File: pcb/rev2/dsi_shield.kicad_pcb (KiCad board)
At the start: 4 copper layers, 68.6 x 53.3 mm, 224 parts, among them CN1 HDMI, CN10 CVBS In, CN2 AX3E41264, CN3 GB042-30S-E1000, CN4 JTAG, CN5 IOH, CN6 POWER, CN7 IOL, CN8 AD, CN9 USB, IC1 XC6SLX9-3TQG144I, IC10 MT46V32M16P-5B:F, IC12 25MHz, IC2 M25P80-VMN6P, IC28 TVP5150AM1PBS, IC3 LV52204MUTBG, IC4 LM26480, IC5 TPS61040, IC6 FT230XS-T, IC8 PRTR5V0U2X, IC9 PRTR5V0U2X, Q1 BSS84, Q2 2N7002, Q3 2N7002, Q4 2N7002, X1 7A-14.31818MAAJ-T

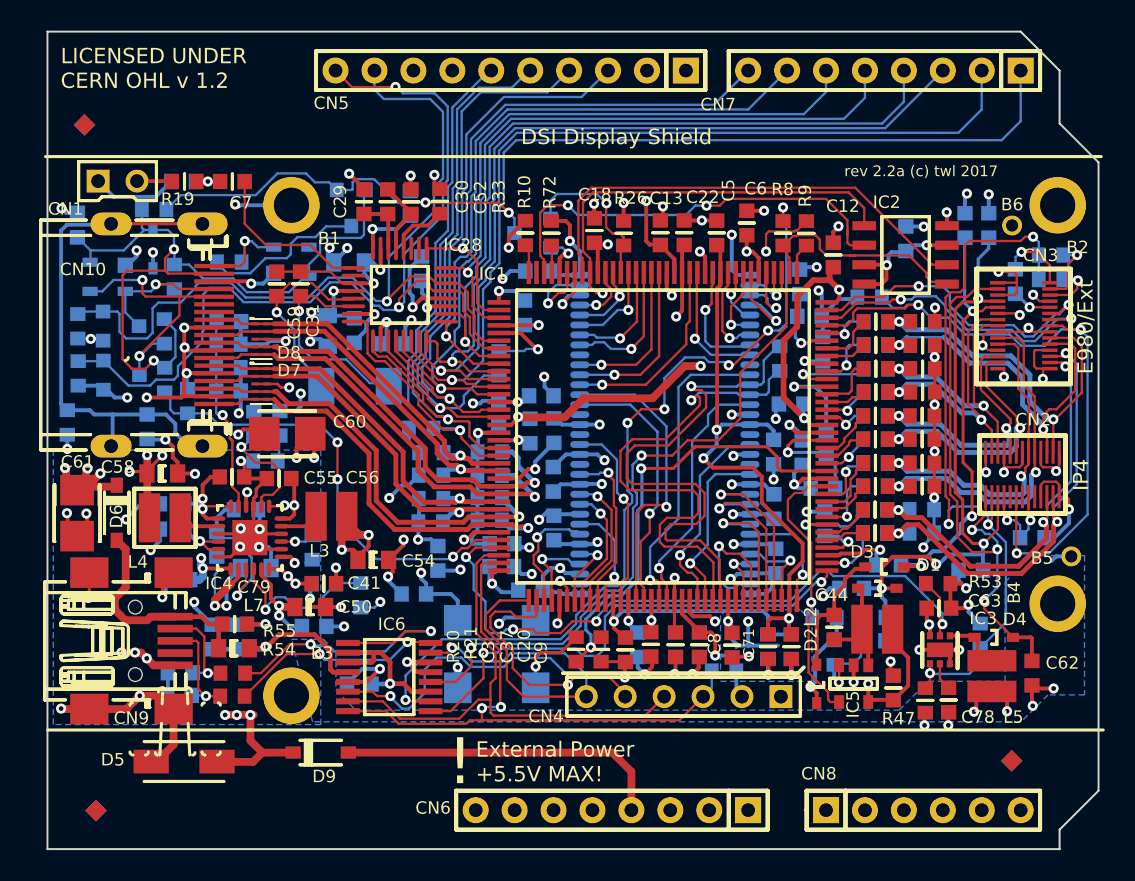
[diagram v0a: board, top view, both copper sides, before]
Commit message: Completed port to KiCad, passes DRC+LVS. NOT MANUFACTURED.
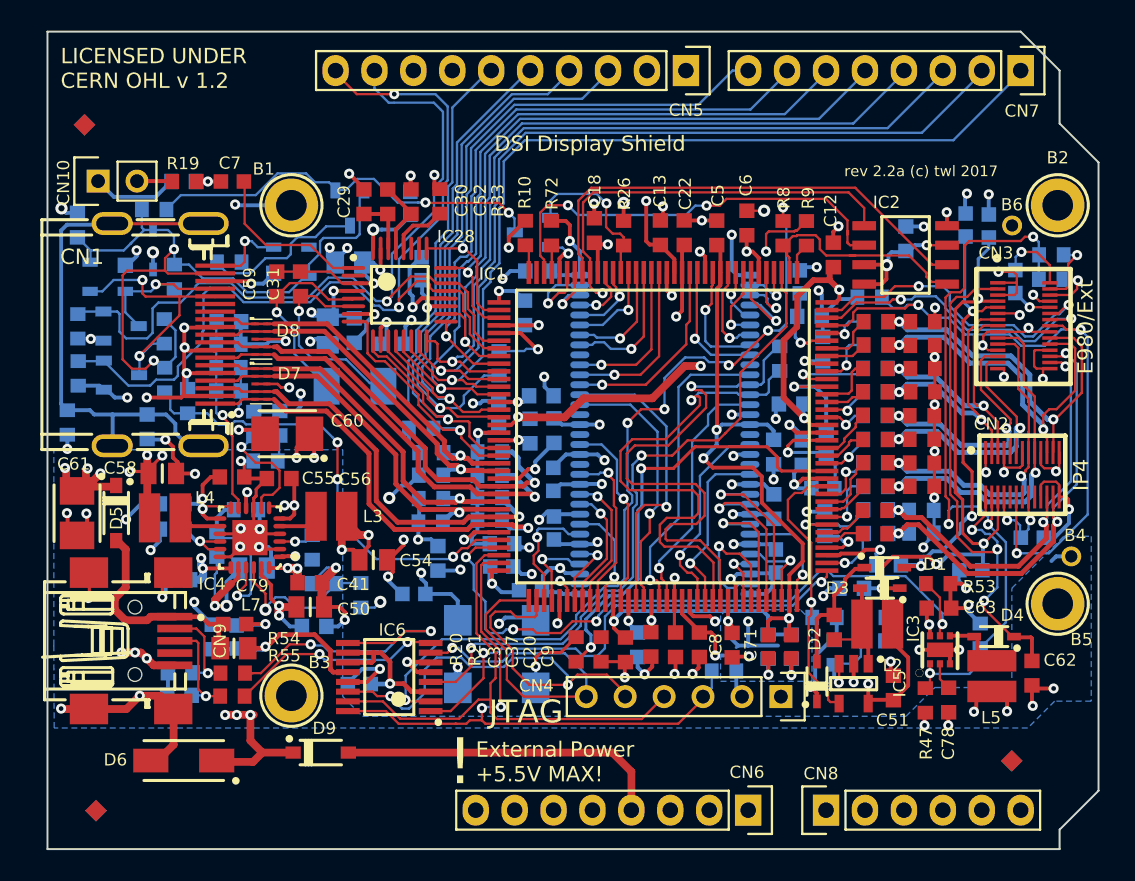
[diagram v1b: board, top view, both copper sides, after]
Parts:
- B1, B2, B3, B4: value Plated Hole -> PLATED_HOLE2.0_PAD3.5; footprint c350h200 -> Pads:c350h200
- B5, B6: value Plated Hole -> PLATED_HOLE0.8_PAD1.3
- C1, C2, C32, C33, C34: value 100n -> CC0603_100NF_100V_10%_X7R; footprint CAPC1608X87N -> CAPC1608X90N
- C10, C12, C13, C15, C16, C18, C20, C21, C22, C23, C25, C27, C28, C3, C35, C36, C37, C38, C4, C40, C5, C8: value 100n -> CC0603_100NF_50V_10%_X7R; footprint CAPC1608X87N -> Capacitors SMD:CAPC1608X87N
- C11, C17, C65, C67, C7, C71, C72, C73, C75, C77, C79, C82, C84, C85, C86: value 100n -> CC0603_100NF_100V_10%_X7R; footprint CAPC1608X87N -> Capacitors SMD:CAPC1608X90N
- C14, C19, C24, C29, C30, C41, C42, C43, C44, C47, C48, C52, C6, C62, C63, C64, C76, C83, C9: value 1u X5R -> CC0603_1UF_50V_10%_X5R; footprint CAPC1608X87N -> Capacitors SMD:CAPC1608X87N
- C26, C39: value 1n -> CC0603_1NF_50V_5%_NP0; footprint CAPC1608X87N -> Capacitors SMD:CAPC1608X90N
- C31, C49, C59: value 22p -> CC0603_22PF_50V_5%_NP0; footprint CAPC1608X87N -> Capacitors SMD:CAPC1608X87N
- C45, C51, C55, C56: value 4.7u X5R -> CC0603_4.7UF_6.3V_10%_X5R; footprint CAPC1608X87N -> Capacitors SMD:CAPC1608X87N
- C46, C50, C54, C58: value 10u X5R -> CC0805_10UF_16V_10%_X5R; footprint INDC2012-0805 -> Capacitors SMD:CAPC2012X135N
- C53: value 8.2p -> CC0603_8.2PF_50V_0.5PF_NP0; footprint CAPC1608X87N -> Capacitors SMD:CAPC1608X87N
- C57: value 6.8p -> CC0603_6.8PF_50V_0.5PF_NP0; footprint CAPC1608X87N -> Capacitors SMD:CAPC1608X87N
- C60, C61: value 47u -> CTE3528-21_47UF_6.3V_10%_LESR0250; footprint TC3528-1411 -> Capacitors SMD:CAPMP3528X210N
- C66, C68, C69, C70: value 10n -> CC0603_10NF_50V_10%_X7R; footprint CAPC1608X87N -> Capacitors SMD:CAPC1608X87N
- C74, C80, C81: value 33p -> CC0603_33PF_50V_5%_NP0; footprint CAPC1608X87N -> Capacitors SMD:CAPC1608X87N
- C78: value 220n -> CC0603_220NF_10V_10%_X7R; footprint CAPC1608X87N -> Capacitors SMD:CAPC1608X87N
- CN1: value HDMI -> MOLEX_500254-1927
- CN10: footprint HDR1X2 -> Pin_Headers:Pin_Header_Straight_1x02
- CN2: footprint IPHONE4_LCD_CONN -> dsi_shield:IPHONE4_LCD_CONN
- CN3: value GB042-30S-E1000 -> CONN_02X15_ALT; footprint GB042-30S-E1000 -> dsi_shield:GB042-30S-E1000
- CN4: footprint HDR1X6 -> Pin_Headers:Pin_Header_Straight_1x06
- CN5: footprint Header 10x1 8.5mm -> Pin_Headers:Pin_Header_Straight_1x10
- CN6: value POWER -> POWER_UNO; footprint Header 8x1 8.5mm -> Pin_Headers:Pin_Header_Straight_1x08
- CN7: footprint Header 8x1 8.5mm -> Pin_Headers:Pin_Header_Straight_1x08
- CN8: footprint Header 6x1 8.5mm -> Pin_Headers:Pin_Header_Straight_1x06
- CN9: value USB -> TYCO_1734035-1; footprint TYCO_1734035-1 -> TYCO SMD:TYCO_1734035-1
- D1, D2, D3, D4: footprint SOD323 -> ICs And Semiconductors SMD:SOD2713X115N
- D10: value BAS170W -> BAS170; footprint SOD323 -> ICs And Semiconductors SMD:SOD2713X115N
- D5: value SMAJ5.0A-E3/61 -> MBR0530PbF; footprint DIOM5226X262N -> ICs And Semiconductors SMD:SOD3715X145N
- D6: value MBR0530PbF -> SMAJ5.0A; footprint SOD3715X145N -> ICs And Semiconductors SMD:DIOM5226X262N
- D7, D8: footprint SOT1176-1 -> dsi_shield:SOT1176-1
- D9: footprint SOD3715X145N -> ICs And Semiconductors SMD:SOD3715X145N
- FTG1, FTG2, FTG3, FTG4, FTG5, FTG6: value Use only in PCB -> FIDUCIAL_TARGET_S100-200; footprint FIDUCIAL_TOP_S100-200 -> Pads:FIDUCIAL_TOP_S100-200
- IC10: footprint TSOP66 -> dsi_shield:TSOP66
- IC12: value 25MHz -> OSC_25MHZ_PERICOM_FNETHE025; footprint OSC_SMD_5x7mm -> ICs And Semiconductors SMD:OSC_PERICOM_FNETHE025
- IC28: footprint TSQFP50P700X700-32L -> dsi_shield:TSQFP50P700X700-32L
- IC3: footprint UDFN6_2X2_065P -> dsi_shield:UDFN6_2X2_065P
- IC4: footprint QFN50P400X400-24W2M -> ICs And Semiconductors SMD:QFN50P400X400X80-25N-S230
- IC5: footprint SOT23-5AL -> ICs And Semiconductors SMD:SOT95P275X110-5N
- IC6: footprint SOP63P600X175-16N -> ICs And Semiconductors SMD:SOP63P600X175-16N
- IC8, IC9: footprint SOT190P230X110-4N -> ICs And Semiconductors SMD:SOT190P230X110-4N
- L1, L6, L7: value 220R@100MHz Ferrite Bead -> IND0805_MURATA_BLM21PG221SN1D; footprint INDC2012-0805 -> Inductors SMD:INDC2012X105N
- L2, L5: footprint IND_PANASONIC_ELLVEG -> dsi_shield:IND_PANASONIC_ELLVEG
- L3, L4: value 2.2 uH -> 2.2uH; footprint IND_PANASONIC_ELLVEG -> dsi_shield:IND_PANASONIC_ELLVEG
- Q1: value BSS84 -> BSS84LT1G; footprint SOT23-3 -> ICs And Semiconductors SMD:SOT95P240X110-3N
- Q2, Q3, Q4: footprint SOT23-3 -> ICs And Semiconductors SMD:SOT95P240X130-3N
- R1: value 10R -> R0603_10R_1%_0.1W_200PPM; footprint RESC1608X55N -> Resistors SMD:RESC1608X55N
- R10, R2, R22, R24, R25, R26, R28, R29, R30, R31, R33, R34, R48, R7, R8, R9: value 3.3k -> R0603_3K3_1%_0.1W_100PPM; footprint RESC1608X55N -> Resistors SMD:RESC1608X55N
- R11, R12, R13, R14, R15, R16, R17, R18: value 51 -> R0603_51R_1%_0.1W_100PPM; footprint RESC1608X55N -> Resistors SMD:RESC1608X55N
- R19, R32, R54, R55: value 33 -> R0603_33R_1%_0.1W_100PPM; footprint RESC1608X55N -> Resistors SMD:RESC1608X55N
- R20: value 180 -> R0603_180R_1%_0.1W_100PPM; footprint RESC1608X55N -> Resistors SMD:RESC1608X55N
- R21: value 220 -> R0603_220R_1%_0.1W_100PPM; footprint RESC1608X55N -> Resistors SMD:RESC1608X55N
- R23, R68, R69: value 1K -> R0603_1K_1%_0.1W_100PPM; footprint RESC1608X55N -> Resistors SMD:RESC1608X55N
- R27: value 1M -> R0603_1M_1%_0.1W_100PPM; footprint RESC1608X55N -> Resistors SMD:RESC1608X55N
- R35, R39, R44, R46, R53: value 100k -> R0603_100K_1%_0.1W_100PPM; footprint RESC1608X55N -> Resistors SMD:RESC1608X55N
- R36: value 280k -> R0603_280K_1%_0.1W_100PPM; footprint RESC1608X55N -> Resistors SMD:RESC1608X55N
- R37: value 200k -> R0603_200K_1%_0.1W_100PPM; footprint RESC1608X55N -> Resistors SMD:RESC1608X55N
- R38: value 750k -> R0603_750K_1%_0.1W_100PPM; footprint RESC1608X55N -> Resistors SMD:RESC1608X55N
- R40: value 187k -> R0603_187K_1%_0.1W_100PPM; footprint RESC1608X55N -> Resistors SMD:RESC1608X55N
- R41: value 464k -> R0603_464K_1%_0.1W_100PPM; footprint RESC1608X55N -> Resistors SMD:RESC1608X55N
- R42: value 27k -> R0603_27K_1%_0.1W_100PPM; footprint RESC1608X55N -> Resistors SMD:RESC1608X55N
- R43: value 178k -> R0603_178K_1%_0.1W_100PPM; footprint RESC1608X55N -> Resistors SMD:RESC1608X55N
- R45: value 560k -> R0603_560K_1%_0.1W_100PPM; footprint RESC1608X55N -> Resistors SMD:RESC1608X55N
- R47, R49, R50: value 10 -> R0603_10R_1%_0.1W_200PPM; footprint RESC1608X55N -> Resistors SMD:RESC1608X55N
- R67: value 100 -> R0603_100R_1%_0.1W_100PPM; footprint RESC1608X55N -> Resistors SMD:RESC1608X55N
- R72: value 0 -> R0603_0R_JUMPER; footprint RESC1608X55N -> Resistors SMD:RESC1608X55N
- RA3, RA4, RC3, RC4, RE3, RE4: value 51R -> R0603_51R_1%_0.1W_100PPM; footprint RESC1608X55N -> Resistors SMD:RESC1608X55N
- RA5, RA52, RB5, RB52, RC5, RC52, RD5, RD52, RE5, RE52: value 160R -> R0603_160R_1%_0.1W_100PPM; footprint RESC1608X55N -> Resistors SMD:RESC1608X55N
- RA51, RA6, RB51, RB6, RC51, RC6, RD51, RD6, RE51, RE6: value 22R -> R0603_22R_1%_0.1W_100PPM; footprint RESC1608X55N -> Resistors SMD:RESC1608X55N
- RB3, RB4: value 51R -> R0603_51R_1%_0.1W_100PPM; footprint RESC1608X55N -> Resistors SMD:RESC1608X55N; moved to F.Cu
- RD3, RD4: value 51R -> R0603_51R_1%_0.1W_100PPM; footprint RESC1608X55N -> Resistors SMD:RESC1608X55N; moved to B.Cu
- X1: value 7A-14.31818MAAJ-T -> XTAL_12MHZ_TXC_7A-14.31818MAAJ-T; footprint XTAL_5.0*3.2 -> ICs And Semiconductors SMD:XTAL_TXC_7A
- moved D5 16.8 mm to (41.6, 131.1), turned to 270 degrees
- moved D6 16.7 mm to (46.0, 147.2), turned to 180 degrees
- moved RA51 6.17 mm to (91.1, 121.6), turned to 0 degrees
- moved RA6 6.17 mm to (91.1, 123.2), turned to 180 degrees
- moved RD5 6.17 mm to (91.1, 132.4)
- moved RD52 6.17 mm to (91.1, 130.9)
- moved RD3 6.17 mm to (94.1, 130.9), turned to 0 degrees
- moved RB52 6.17 mm to (91.1, 124.7)
- moved RA4 6.16 mm to (94.2, 123.2), turned to 180 degrees
- moved RA3 6.16 mm to (94.2, 121.7), turned to 0 degrees
- moved RA5 6.16 mm to (91.1, 123.2)
- moved RA52 6.16 mm to (91.1, 121.7)
- moved RE6 6.16 mm to (91.1, 129.3), turned to 180 degrees
- moved RD6 6.15 mm to (91.2, 132.4), turned to 180 degrees
- moved RE3 6.15 mm to (94.1, 127.8), turned to 0 degrees
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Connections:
- net CFG_CCLK renamed /FPGA/CFG_CCLK
- net CFG_DONE renamed /FPGA/CFG_DONE
- net CFG_M0 renamed /FPGA/CFG_M0
- net CFG_MISO renamed /FPGA/CFG_MISO
- net CFG_MOSI renamed /FPGA/CFG_MOSI
- net CLK_25MHZ renamed /CLK_25MHZ
- net DBG_RX renamed /FPGA/DBG_RX
- net DBG_TX renamed /FPGA/DBG_TX
- net DSI_GPIO0 renamed /CONN/DSI_GPIO0
- net DSI_GPIO1 renamed /CONN/DSI_GPIO1
- net DSI_HS_N2 renamed /FPGA/DSI_HS_N2
- net DSI_HS_P2 renamed /FPGA/DSI_HS_P2
- net DSI_RESET_N renamed /CONN/DSI_RESET_N
- net HDMI_CEC renamed /HDMI_IN/HDMI_CEC
- net HDMI_HPD renamed /HDMI_IN/HDMI_HPD
- net HOST_CS renamed /HOST_CS
- net HOST_D0 renamed /HOST_D0
- net HOST_D1 renamed /HOST_D1
- net HOST_D2 renamed /HOST_D2
- net HOST_D3 renamed /HOST_D3
- net HOST_D4 renamed /HOST_D4
- net HOST_D5 renamed /HOST_D5
- net HOST_D6 renamed /HOST_D6
- net HOST_D7 renamed /HOST_D7
- net HOST_WE renamed /HOST_WE
- net HPD_EN renamed /FPGA/HPD_EN
- net LCD_BL_A renamed /CONN/LCD_BL_A
- net NetC30_1 renamed Net-(C30-Pad1)
- net NetC31_1 renamed Net-(C31-Pad1)
- net NetC44_1 renamed Net-(C44-Pad1)
- net NetC44_2 renamed Net-(C44-Pad2)
- net NetC59_1 renamed Net-(C59-Pad1)
- net NetC78_1 renamed Net-(C78-Pad1)
- net NetC7_2 renamed Net-(C7-Pad2)
- net NetCN6_4 renamed Net-(CN6-Pad4)
- net NetD4_2 renamed Net-(D4-Pad2)
- net NetIC1_14 renamed Net-(IC1-Pad14)
- net NetIC4_14 renamed Net-(IC4-Pad14)
- net NetIC4_5 renamed Net-(IC4-Pad5)
- net NetQ1_1 renamed Net-(Q1-Pad1)
- net NetQ1_3 renamed Net-(Q1-Pad3)
- net SDRAM_A0 renamed /DDR/SDRAM_A0
- net SDRAM_A1 renamed /DDR/SDRAM_A1
- net SDRAM_A10 renamed /DDR/SDRAM_A10
- net SDRAM_A11 renamed /DDR/SDRAM_A11
- net SDRAM_A12 renamed /DDR/SDRAM_A12
- net SDRAM_A2 renamed /DDR/SDRAM_A2
- net SDRAM_A3 renamed /DDR/SDRAM_A3
- net SDRAM_A4 renamed /DDR/SDRAM_A4
- net SDRAM_A5 renamed /DDR/SDRAM_A5
- net SDRAM_A6 renamed /DDR/SDRAM_A6
- net SDRAM_A7 renamed /DDR/SDRAM_A7
- net SDRAM_A8 renamed /DDR/SDRAM_A8
- net SDRAM_A9 renamed /DDR/SDRAM_A9
- net SDRAM_BA0 renamed /DDR/SDRAM_BA0
- net SDRAM_BA1 renamed /DDR/SDRAM_BA1
- net SDRAM_CAS_N renamed /DDR/SDRAM_CAS_N
- net SDRAM_CKE renamed /DDR/SDRAM_CKE
- net SDRAM_CS_N renamed /DDR/SDRAM_CS_N
- net SDRAM_DQ0 renamed /DDR/SDRAM_DQ0
- net SDRAM_DQ1 renamed /DDR/SDRAM_DQ1
- net SDRAM_DQ10 renamed /DDR/SDRAM_DQ10
- net SDRAM_DQ11 renamed /DDR/SDRAM_DQ11
- net SDRAM_DQ12 renamed /DDR/SDRAM_DQ12
- net SDRAM_DQ13 renamed /DDR/SDRAM_DQ13
- net SDRAM_DQ14 renamed /DDR/SDRAM_DQ14
- net SDRAM_DQ15 renamed /DDR/SDRAM_DQ15
- net SDRAM_DQ2 renamed /DDR/SDRAM_DQ2
- net SDRAM_DQ3 renamed /DDR/SDRAM_DQ3
- net SDRAM_DQ4 renamed /DDR/SDRAM_DQ4
- net SDRAM_DQ5 renamed /DDR/SDRAM_DQ5
- net SDRAM_DQ6 renamed /DDR/SDRAM_DQ6
- net SDRAM_DQ7 renamed /DDR/SDRAM_DQ7
- net SDRAM_DQ8 renamed /DDR/SDRAM_DQ8
- net SDRAM_DQ9 renamed /DDR/SDRAM_DQ9
- net SDRAM_DQM0 renamed /DDR/SDRAM_DQM0
- net SDRAM_DQM1 renamed /DDR/SDRAM_DQM1
- net SDRAM_DQS0 renamed /DDR/SDRAM_DQS0
- net SDRAM_DQS1 renamed /DDR/SDRAM_DQS1
- net SDRAM_RAS_N renamed /DDR/SDRAM_RAS_N
- net SDRAM_WE_N renamed /DDR/SDRAM_WE_N
- net TCK renamed /FPGA/TCK
- net TDI renamed /FPGA/TDI
- net TDO renamed /FPGA/TDO
- B5 pad 1: P5V_IN -> +5V
- C1 pad 1: GND -> LCD_PVDD
- C1 pad 2: LCD_PVDRV -> GND
- C10 pad 1: P3V3 -> +3V3
- C11 pad 1: P2V5 -> +2V5
- C12 pad 1: P3V3 -> +3V3
- C13 pad 1: P3V3 -> +3V3
- C14 pad 1: P3V3 -> +3V3
- C15 pad 1: P3V3 -> +3V3
- C16 pad 1: P3V3 -> +3V3
- C17 pad 1: P3V3 -> +3V3
- C18 pad 1: P2V5 -> +2V5
- C19 pad 1: P1V2 -> +1V2
- C2 pad 1: GND -> +1V8
- C2 pad 2: P1V8 -> GND
- C20 pad 1: P1V2 -> +1V2
- C21 pad 1: P1V2 -> +1V2
- C22 pad 1: P1V2 -> +1V2
- C23 pad 1: P1V2 -> +1V2
- C24 pad 1: P1V8 -> +1V8
- C25 pad 1: P1V8 -> +1V8
- C26 pad 1: P1V8 -> +1V8
- C27 pad 1: HDMI_P5V -> /HDMI_IN/HDMI_P5V
- C28 pad 1: GND -> Net-(C28-Pad1)
- C28 pad 2: NetC28_2 -> GND
- C29 pad 1: VI_GND -> Net-(C29-Pad1)
- C29 pad 2: NetC29_2 -> GNDA
- C3 pad 1: DDR_VREF -> /DDR/DDR_VREF
- C30 pad 2: NetC29_2 -> Net-(C29-Pad1)
- C31 pad 2: VI_GND -> GNDA
- C32 pad 1: GND -> LCD_PVDD
- C32 pad 2: LCD_MVDRV -> GND
- C33 pad 1: GND -> LCD_MVDD
- C33 pad 2: LCD_PVDRV -> GND
- C34 pad 1: GND -> +1V8
- C34 pad 2: P1V8 -> GND
- C35 pad 1: P3V3 -> +3V3
- C36 pad 1: P3V3 -> +3V3
- C37 pad 1: P2V5 -> +2V5
- C38 pad 1: P3V3 -> +3V3
- C39 pad 1: P1V8 -> +1V8
- C4 pad 1: DDR_VREF -> /DDR/DDR_VREF
- C40 pad 1: P1V8 -> +1V8
- C41 pad 1: P3V3 -> +3V3
- C42 pad 2: P5V_IN -> +5V
- C43 pad 2: P5V_IN -> +5V
- C45 pad 1: LCD_MVDRV -> LCD_MVDD
- C46 pad 1: P1V2 -> +1V2
- C47 pad 1: P1V8 -> +1V8
- C48 pad 1: LCD_PVDRV -> LCD_PVDD
- C49 pad 1: LCD_PVDRV -> LCD_PVDD
- C49 pad 2: LCD_BOOST_FB -> /PSU/LCD_BOOST_FB
- C5 pad 1: DDR_VREF -> /DDR/DDR_VREF
- C50 pad 1: P2V5 -> +2V5
- C51 pad 1: P3V3 -> +3V3
- C52 pad 1: VI_GND -> GNDA
- C53 pad 1: P1V8 -> +1V8
- C53 pad 2: NetC53_2 -> Net-(C53-Pad2)
- C54 pad 1: P1V8 -> +1V8
- C55 pad 1: P5V_IN -> +5V
- C56 pad 1: P5V_IN -> +5V
- C57 pad 1: P3V3 -> +3V3
- C57 pad 2: NetC57_2 -> Net-(C57-Pad2)
- C58 pad 1: P3V3 -> +3V3
- C59 pad 2: VI_GND -> GNDA
- C6 pad 1: P2V5 -> +2V5
- C60 pad 1: P5V_IN -> +5V
- C61 pad 1: P5V_IN -> +5V
- C63 pad 1: P3V3 -> +3V3
- C64 pad 1: GND -> +2V5
- C64 pad 2: P2V5 -> GND
- C65 pad 1: DDR_VREF -> +2V5
- C65 pad 2: P2V5 -> /DDR/DDR_VREF
- C66 pad 1: GND -> +2V5
- C66 pad 2: P2V5 -> GND
- C67 pad 1: GND -> +2V5
- C67 pad 2: P2V5 -> GND
- C68 pad 1: GND -> +2V5
- C68 pad 2: P2V5 -> GND
- C69 pad 1: GND -> +2V5
- C69 pad 2: P2V5 -> GND
- C7 pad 1: NetC7_1 -> Net-(C7-Pad1)
- C70 pad 1: GND -> +2V5
- C70 pad 2: P2V5 -> GND
- C71 pad 1: GND -> /DDR/DDR_VREF
- C71 pad 2: DDR_VREF -> GND
- C72 pad 1: P2V5 -> +2V5
- C73 pad 1: P2V5 -> +2V5
- C74 pad 1: NetC57_2 -> Net-(C57-Pad2)
- C75 pad 1: P2V5 -> +2V5
- C76 pad 1: NetC76_1 -> GND
- C76 pad 2: GND -> Net-(C76-Pad2)
- C77 pad 1: NetC76_1 -> GND
- C77 pad 2: GND -> Net-(C76-Pad2)
- C79 pad 1: NetC79_1 -> Net-(C79-Pad1)
- C8 pad 1: P2V5 -> +2V5
- C80 pad 1: NetC80_1 -> Net-(C80-Pad1)
- C81 pad 1: NetC81_1 -> Net-(C81-Pad1)
- C82 pad 1: GND -> Net-(C82-Pad1)
- C82 pad 2: NetC82_2 -> GND
- C83 pad 1: VI_AVDD -> VDDA
- C83 pad 2: VI_GND -> GNDA
- C84 pad 1: VI_GND -> VDDA
- C84 pad 2: VI_AVDD -> GNDA
- C85 pad 1: GND -> +1V8
- C85 pad 2: P1V8 -> GND
- C86 pad 1: GND -> +3V3
- C86 pad 2: P3V3 -> GND
- C9 pad 1: P3V3 -> +3V3
- CN1 pad 1: TMDS2_P -> /HDMI_IN/TMDS2_P
- CN1 pad 10: TMDS_CLK_P -> /HDMI_IN/TMDS_CLK_P
- CN1 pad 12: TMDS_CLK_N -> /HDMI_IN/TMDS_CLK_N
- CN1 pad 14: (no net) -> Net-(CN1-Pad14)
- CN1 pad 15: HDMI_SCL -> /HDMI_IN/HDMI_SCL
- CN1 pad 16: HDMI_SDA -> /HDMI_IN/HDMI_SDA
- CN1 pad 18: HDMI_P5V -> /HDMI_IN/HDMI_P5V
- CN1 pad 3: TMDS2_N -> /HDMI_IN/TMDS2_N
- CN1 pad 4: TMDS1_P -> /HDMI_IN/TMDS1_P
- CN1 pad 6: TMDS1_N -> /HDMI_IN/TMDS1_N
- CN1 pad 7: TMDS0_P -> /HDMI_IN/TMDS0_P
- CN1 pad 9: TMDS0_N -> /HDMI_IN/TMDS0_N
- CN1 pad SHIE: NetC28_2 -> Net-(C28-Pad1)
- CN10 pad 1: VI_GND -> GNDA
- CN10 pad 2: NetCN10_2 -> /COMP_IN/CVBS_IN
- CN2 pad 10: (no net) -> Net-(CN2-Pad10)
- CN2 pad 11: DSI_L1_N -> /CONN/DSI_L1_N
- CN2 pad 14: (no net) -> Net-(CN2-Pad14)
- CN2 pad 15: DSI_CLK_P -> /CONN/DSI_CLK_P
- CN2 pad 16: P1V8 -> +1V8
- CN2 pad 17: DSI_CLK_N -> /CONN/DSI_CLK_N
- CN2 pad 18: (no net) -> Net-(CN2-Pad18)
- CN2 pad 21: DSI_L2_N -> /CONN/DSI_L2_N
- CN2 pad 22: DSI_L3_P -> /CONN/DSI_L3_P
- CN2 pad 23: DSI_L2_P -> /CONN/DSI_L2_P
- CN2 pad 24: DSI_L3_N -> /CONN/DSI_L3_N
- CN2 pad 3: DSI_L0_N -> /CONN/DSI_L0_N
- CN2 pad 4: LCD_BL_FB -> /CONN/LCD_BL_FB
- CN2 pad 5: DSI_L0_P -> /CONN/DSI_L0_P
- CN2 pad 6: LCD_PVDRV -> LCD_PVDD
- CN2 pad 8: P1V8 -> +1V8
- CN2 pad 9: DSI_L1_P -> /CONN/DSI_L1_P
- CN3 pad 10: DSI_CLK_N -> /CONN/DSI_CLK_N
- CN3 pad 11: DSI_CLK_P -> /CONN/DSI_CLK_P
- CN3 pad 13: DSI_L1_P -> /CONN/DSI_L1_P
- CN3 pad 14: DSI_L1_N -> /CONN/DSI_L1_N
- CN3 pad 17: DSI_L3_P -> /CONN/DSI_L3_P
- CN3 pad 18: DSI_L3_N -> /CONN/DSI_L3_N
- CN3 pad 20: DSI_L2_N -> /CONN/DSI_L2_N
- CN3 pad 21: DSI_L2_P -> /CONN/DSI_L2_P
- CN3 pad 26: P1V8 -> +1V8
- CN3 pad 28: NetCN3_28 -> Net-(CN3-Pad28)
- CN3 pad 29: NetCN3_29 -> Net-(CN3-Pad29)
- CN3 pad 4: LCD_PVDRV -> LCD_PVDD
- CN3 pad 5: LCD_MVDRV -> LCD_MVDD
- CN3 pad 7: DSI_L0_N -> /CONN/DSI_L0_N
- CN3 pad 8: DSI_L0_P -> /CONN/DSI_L0_P
- CN4 pad 2: P3V3 -> +3V3
- CN4 pad 3: TMS -> /FPGA/TMS
- CN5 pad 1: (no net) -> Net-(CN5-Pad1)
- CN5 pad 10: SCL -> /SCL
- CN5 pad 2: (no net) -> Net-(CN5-Pad2)
- CN5 pad 4: HOST_RD -> /HOST_RD
- CN5 pad 6: HOST_A0 -> /HOST_A0
- CN5 pad 8: (no net) -> Net-(CN5-Pad8)
- CN5 pad 9: SDA -> /SDA
- CN6 pad 1: (no net) -> Net-(CN6-Pad1)
- CN6 pad 5: (no net) -> Net-(CN6-Pad5)
- CN6 pad 6: (no net) -> Net-(CN6-Pad6)
- CN6 pad 7: (no net) -> Net-(CN6-Pad7)
- CN6 pad 8: (no net) -> Net-(CN6-Pad8)
- CN8 pad 1: (no net) -> Net-(CN8-Pad1)
- CN8 pad 2: (no net) -> Net-(CN8-Pad2)
- CN8 pad 3: (no net) -> Net-(CN8-Pad3)
- CN8 pad 4: (no net) -> Net-(CN8-Pad4)
- CN8 pad 5: (no net) -> Net-(CN8-Pad5)
- CN8 pad 6: (no net) -> Net-(CN8-Pad6)
- CN9 pad 1: NetC79_1 -> Net-(C79-Pad1)
- CN9 pad 2: NetC80_1 -> Net-(C80-Pad1)
- CN9 pad 3: NetC81_1 -> Net-(C81-Pad1)
- CN9 pad 4: (no net) -> Net-(CN9-Pad4)
- D1 pad 2: LCD_MVDRV -> LCD_MVDD
- D10 pad 1: HDMI_P5V -> /HDMI_IN/HDMI_P5V
- D10 pad 2: P3V3 -> +3V3
- D3 pad 1: LCD_PVDRV -> LCD_PVDD
- D5 pad 1: P5V_IN -> +5V
- D5 pad 2: GND -> Net-(C79-Pad1)
- D6 pad 1: P5V_IN -> +5V
- D6 pad 2: NetC79_1 -> GND
- D7 pad 1: TMDS1_N -> /HDMI_IN/TMDS1_N
- D7 pad 10: TMDS1_N -> /HDMI_IN/TMDS1_N
- D7 pad 2: TMDS1_P -> /HDMI_IN/TMDS1_P
- D7 pad 4: TMDS2_N -> /HDMI_IN/TMDS2_N
- D7 pad 5: TMDS2_P -> /HDMI_IN/TMDS2_P
- D7 pad 6: TMDS2_P -> /HDMI_IN/TMDS2_P
- D7 pad 7: TMDS2_N -> /HDMI_IN/TMDS2_N
- D7 pad 9: TMDS1_P -> /HDMI_IN/TMDS1_P
- D8 pad 1: TMDS_CLK_N -> /HDMI_IN/TMDS_CLK_N
- D8 pad 10: TMDS_CLK_N -> /HDMI_IN/TMDS_CLK_N
- D8 pad 2: TMDS_CLK_P -> /HDMI_IN/TMDS_CLK_P
- D8 pad 4: TMDS0_N -> /HDMI_IN/TMDS0_N
- D8 pad 5: TMDS0_P -> /HDMI_IN/TMDS0_P
- D8 pad 6: TMDS0_P -> /HDMI_IN/TMDS0_P
- D8 pad 7: TMDS0_N -> /HDMI_IN/TMDS0_N
- D8 pad 9: TMDS_CLK_P -> /HDMI_IN/TMDS_CLK_P
- D9 pad 1: P5V_IN -> +5V
- IC1 pad 10: DSI_HS_CLK_P -> /FPGA/DSI_HS_CLK_P
- IC1 pad 100: TMDS1_P -> /HDMI_IN/TMDS1_P
- IC1 pad 101: TMDS2_N -> /HDMI_IN/TMDS2_N
- IC1 pad 102: TMDS2_P -> /HDMI_IN/TMDS2_P
- IC1 pad 103: P3V3 -> +3V3
- IC1 pad 104: HPD_NOTIF -> /FPGA/HPD_NOTIF
- IC1 pad 105: BL_DIM -> /FPGA/BL_DIM
- IC1 pad 107: TMS -> /FPGA/TMS
- IC1 pad 11: DSI_LP_CLK_P -> /FPGA/DSI_LP_CLK_P
- IC1 pad 12: LCD_PWREN -> /FPGA/LCD_PWREN
- IC1 pad 120: DDR_VREF -> /DDR/DDR_VREF
- IC1 pad 122: P2V5 -> +2V5
- IC1 pad 125: P2V5 -> +2V5
- IC1 pad 128: P1V2 -> +1V2
- IC1 pad 129: P3V3 -> +3V3
- IC1 pad 133: SDRAM_CLK_N -> /DDR/SDRAM_CLK_N
- IC1 pad 134: SDRAM_CLK_P -> /DDR/SDRAM_CLK_P
- IC1 pad 135: P2V5 -> +2V5
- IC1 pad 143: DDR_VREF -> /DDR/DDR_VREF
- IC1 pad 15: DSI_LP_N1 -> /FPGA/DSI_LP_N1
- IC1 pad 16: DSI_HS_N1 -> /FPGA/DSI_HS_N1
- IC1 pad 17: DSI_HS_P1 -> /FPGA/DSI_HS_P1
- IC1 pad 18: P1V8 -> +1V8
- IC1 pad 19: P1V2 -> +1V2
- IC1 pad 2: DSI_LP_N3 -> /FPGA/DSI_LP_N3
- IC1 pad 20: P3V3 -> +3V3
- IC1 pad 21: DSI_LP_P1 -> /FPGA/DSI_LP_P1
- IC1 pad 22: DSI_LP_N0 -> /FPGA/DSI_LP_N0
- IC1 pad 23: DSI_HS_N0 -> /FPGA/DSI_HS_N0
- IC1 pad 24: DSI_HS_P0 -> /FPGA/DSI_HS_P0
- IC1 pad 26: DSI_LP_P0 -> /FPGA/DSI_LP_P0
- IC1 pad 27: DSI_LP_N2 -> /FPGA/DSI_LP_N2
- IC1 pad 28: P1V2 -> +1V2
- IC1 pad 31: P1V8 -> +1V8
- IC1 pad 32: DSI_LP_P2 -> /FPGA/DSI_LP_P2
- IC1 pad 36: P3V3 -> +3V3
- IC1 pad 37: NetIC1_37 -> Net-(IC1-Pad37)
- IC1 pad 38: CFG_CS -> /FPGA/CFG_CS
- IC1 pad 4: P1V8 -> +1V8
- IC1 pad 42: P2V5 -> +2V5
- IC1 pad 47: DDR_VREF -> /DDR/DDR_VREF
- IC1 pad 5: DSI_HS_N3 -> /FPGA/DSI_HS_N3
- IC1 pad 52: P1V2 -> +1V2
- IC1 pad 53: P3V3 -> +3V3
- IC1 pad 6: DSI_HS_P3 -> /FPGA/DSI_HS_P3
- IC1 pad 63: P2V5 -> +2V5
- IC1 pad 7: DSI_LP_P3 -> /FPGA/DSI_LP_P3
- IC1 pad 72: NetIC1_72 -> Net-(IC1-Pad72)
- IC1 pad 76: P3V3 -> +3V3
- IC1 pad 78: SDA -> /SDA
- IC1 pad 79: SCL -> /SCL
- IC1 pad 8: DSI_LP_CLK_N -> /FPGA/DSI_LP_CLK_N
- IC1 pad 86: P3V3 -> +3V3
- IC1 pad 88: HOST_RD -> /HOST_RD
- IC1 pad 89: P1V2 -> +1V2
- IC1 pad 9: DSI_HS_CLK_N -> /FPGA/DSI_HS_CLK_N
- IC1 pad 90: P3V3 -> +3V3
- IC1 pad 93: HOST_A0 -> /HOST_A0
- IC1 pad 94: TMDS_CLK_N -> /HDMI_IN/TMDS_CLK_N
- IC1 pad 95: TMDS_CLK_P -> /HDMI_IN/TMDS_CLK_P
- IC1 pad 97: TMDS0_N -> /HDMI_IN/TMDS0_N
- IC1 pad 98: TMDS0_P -> /HDMI_IN/TMDS0_P
- IC1 pad 99: TMDS1_N -> /HDMI_IN/TMDS1_N
- IC10 pad 1: P2V5 -> +2V5
- IC10 pad 15: P2V5 -> +2V5
- IC10 pad 18: P2V5 -> +2V5
- IC10 pad 3: P2V5 -> +2V5
- IC10 pad 33: P2V5 -> +2V5
- IC10 pad 45: SDRAM_CLK_P -> /DDR/SDRAM_CLK_P
- IC10 pad 46: SDRAM_CLK_N -> /DDR/SDRAM_CLK_N
- IC10 pad 49: DDR_VREF -> /DDR/DDR_VREF
- IC10 pad 55: P2V5 -> +2V5
- IC10 pad 61: P2V5 -> +2V5
- IC10 pad 9: P2V5 -> +2V5
- IC12 pad 1: P3V3 -> +3V3
- IC12 pad 4: P3V3 -> +3V3
- IC2 pad 1: CFG_CS -> /FPGA/CFG_CS
- IC2 pad 3: P3V3 -> +3V3
- IC2 pad 7: P3V3 -> +3V3
- IC2 pad 8: P3V3 -> +3V3
- IC28 pad 10: P3V3 -> +3V3
- IC28 pad 11: HOST_RD -> /HOST_RD
- IC28 pad 2: (no net) -> Net-(IC28-Pad2)
- IC28 pad 20: P1V8 -> +1V8
- IC28 pad 21: SCL -> /SCL
- IC28 pad 22: SDA -> /SDA
- IC28 pad 23: (no net) -> Net-(IC28-Pad23)
- IC28 pad 26: (no net) -> Net-(IC28-Pad26)
- IC28 pad 27: (no net) -> Net-(IC28-Pad27)
- IC28 pad 28: NetIC28_28 -> Net-(IC28-Pad28)
- IC28 pad 3: VI_GND -> GNDA
- IC28 pad 30: NetC29_2 -> Net-(C29-Pad1)
- IC28 pad 31: VI_GND -> GNDA
- IC28 pad 32: VI_AVDD -> VDDA
- IC28 pad 4: VI_AVDD -> VDDA
- IC28 pad 7: VI_GND -> GNDA
- IC28 pad 8: HOST_A0 -> /HOST_A0
- IC3 pad 1: LCD_BL_FB -> /CONN/LCD_BL_FB
- IC3 pad 5: BL_DIM -> /FPGA/BL_DIM
- IC3 pad 6: P3V3 -> +3V3
- IC4 pad 1: P5V_IN -> +5V
- IC4 pad 10: P5V_IN -> +5V
- IC4 pad 11: NetC57_2 -> Net-(C57-Pad2)
- IC4 pad 12: P5V_IN -> +5V
- IC4 pad 13: P5V_IN -> +5V
- IC4 pad 16: P5V_IN -> +5V
- IC4 pad 17: P5V_IN -> +5V
- IC4 pad 19: P1V8 -> +1V8
- IC4 pad 20: P1V2 -> +1V2
- IC4 pad 21: NetIC4_21 -> Net-(IC4-Pad21)
- IC4 pad 22: NetIC4_22 -> Net-(IC4-Pad22)
- IC4 pad 23: P2V5 -> +2V5
- IC4 pad 24: P3V3 -> +3V3
- IC4 pad 3: NetIC4_3 -> Net-(IC4-Pad3)
- IC4 pad 6: P5V_IN -> +5V
- IC4 pad 7: P5V_IN -> +5V
- IC4 pad 8: NetC53_2 -> Net-(C53-Pad2)
- IC5 pad 3: LCD_BOOST_FB -> /PSU/LCD_BOOST_FB
- IC5 pad 4: LCD_PWREN -> /FPGA/LCD_PWREN
- IC5 pad 5: P3V3 -> +3V3
- IC6 pad 10: NetC82_2 -> Net-(C82-Pad1)
- IC6 pad 11: NetC82_2 -> Net-(C82-Pad1)
- IC6 pad 12: NetC76_1 -> Net-(C76-Pad2)
- IC6 pad 16: TMS -> /FPGA/TMS
- IC6 pad 2: CPU_RST -> /CPU_RST_N
- IC6 pad 3: NetC82_2 -> Net-(C82-Pad1)
- IC6 pad 8: NetIC6_8 -> Net-(IC6-Pad8)
- IC6 pad 9: NetIC6_9 -> Net-(IC6-Pad9)
- IC8 pad 3: (no net) -> Net-(IC8-Pad3)
- IC8 pad 4: HDMI_P5V -> /HDMI_IN/HDMI_P5V
- IC9 pad 2: HDMI_SDA -> /HDMI_IN/HDMI_SDA
- IC9 pad 3: HDMI_SCL -> /HDMI_IN/HDMI_SCL
- IC9 pad 4: HDMI_P5V -> /HDMI_IN/HDMI_P5V
- L1 pad 2: VI_GND -> GNDA
- L2 pad 1: P3V3 -> +3V3
- L3 pad 2: P1V8 -> +1V8
- L4 pad 2: P3V3 -> +3V3
- L5 pad 1: P3V3 -> +3V3
- L6 pad 1: P1V8 -> +1V8
- L6 pad 2: VI_AVDD -> VDDA
- L7 pad 1: NetC79_1 -> Net-(C79-Pad1)
- L7 pad 2: NetC76_1 -> Net-(C76-Pad2)
- Q1 pad 2: HDMI_P5V -> /HDMI_IN/HDMI_P5V
- Q3 pad 1: P3V3 -> +3V3
- Q3 pad 2: SCL -> /SCL
- Q3 pad 3: HDMI_SCL -> /HDMI_IN/HDMI_SCL
- Q4 pad 1: P3V3 -> +3V3
- Q4 pad 2: SDA -> /SDA
- Q4 pad 3: HDMI_SDA -> /HDMI_IN/HDMI_SDA
- R1 pad 1: LCD_BL_FB -> /CONN/LCD_BL_FB
- R10 pad 1: P2V5 -> Net-(IC1-Pad72)
- R10 pad 2: NetIC1_72 -> +2V5
- R11 pad 1: TMDS2_N -> +3V3
- R11 pad 2: P3V3 -> /HDMI_IN/TMDS2_N
- R12 pad 1: TMDS2_P -> +3V3
- R12 pad 2: P3V3 -> /HDMI_IN/TMDS2_P
- R13 pad 1: TMDS_CLK_P -> +3V3
- R13 pad 2: P3V3 -> /HDMI_IN/TMDS_CLK_P
- R14 pad 1: TMDS_CLK_N -> +3V3
- R14 pad 2: P3V3 -> /HDMI_IN/TMDS_CLK_N
- R15 pad 1: TMDS1_N -> +3V3
- R15 pad 2: P3V3 -> /HDMI_IN/TMDS1_N
- R16 pad 1: TMDS1_P -> +3V3
- R16 pad 2: P3V3 -> /HDMI_IN/TMDS1_P
- R17 pad 1: TMDS0_P -> +3V3
- R17 pad 2: P3V3 -> /HDMI_IN/TMDS0_P
- R18 pad 1: TMDS0_N -> +3V3
- R18 pad 2: P3V3 -> /HDMI_IN/TMDS0_N
- R19 pad 1: NetC7_1 -> /COMP_IN/CVBS_IN
- R19 pad 2: NetCN10_2 -> Net-(C7-Pad1)
- R22 pad 1: HDMI_P5V -> /HDMI_IN/HDMI_P5V
- R24 pad 1: HDMI_SCL -> /HDMI_IN/HDMI_P5V
- R24 pad 2: HDMI_P5V -> /HDMI_IN/HDMI_SCL
- R25 pad 1: SCL -> +3V3
- R25 pad 2: P3V3 -> /SCL
- R27 pad 1: GND -> Net-(C28-Pad1)
- R27 pad 2: NetC28_2 -> GND
- R28 pad 1: HDMI_SDA -> /HDMI_IN/HDMI_P5V
- R28 pad 2: HDMI_P5V -> /HDMI_IN/HDMI_SDA
- R29 pad 1: SDA -> +3V3
- R29 pad 2: P3V3 -> /SDA
- R30 pad 1: HPD_NOTIF -> /HDMI_IN/HDMI_P5V
- R30 pad 2: HDMI_P5V -> /FPGA/HPD_NOTIF
- R31 pad 1: GND -> /FPGA/HPD_NOTIF
- R31 pad 2: HPD_NOTIF -> GND
- R32 pad 1: NetC7_1 -> Net-(C7-Pad1)
- R32 pad 2: VI_GND -> GNDA
- R33 pad 1: NetIC28_28 -> +3V3
- R33 pad 2: P3V3 -> Net-(IC28-Pad28)
- R34 pad 1: HOST_A0 -> +3V3
- R34 pad 2: P3V3 -> /HOST_A0
- R35 pad 1: P5V_IN -> Net-(IC4-Pad3)
- R35 pad 2: NetIC4_3 -> +5V
- R36 pad 1: NetIC4_21 -> +1V2
- R36 pad 2: P1V2 -> Net-(IC4-Pad21)
- R37 pad 1: GND -> Net-(IC4-Pad21)
- R37 pad 2: NetIC4_21 -> GND
- R38 pad 1: NetIC4_22 -> +2V5
- R38 pad 2: P2V5 -> Net-(IC4-Pad22)
- R39 pad 1: LCD_BOOST_FB -> LCD_PVDD
- R39 pad 2: LCD_PVDRV -> /PSU/LCD_BOOST_FB
- R40 pad 1: GND -> Net-(IC4-Pad22)
- R40 pad 2: NetIC4_22 -> GND
- R41 pad 1: NetC53_2 -> +1V8
- R41 pad 2: P1V8 -> Net-(C53-Pad2)
- R42 pad 1: GND -> /PSU/LCD_BOOST_FB
- R42 pad 2: LCD_BOOST_FB -> GND
- R43 pad 1: GND -> Net-(C53-Pad2)
- R43 pad 2: NetC53_2 -> GND
- R44 pad 1: GND -> /FPGA/LCD_PWREN
- R44 pad 2: LCD_PWREN -> GND
- R45 pad 1: NetC57_2 -> +3V3
- R45 pad 2: P3V3 -> Net-(C57-Pad2)
- R46 pad 1: GND -> Net-(C57-Pad2)
- R46 pad 2: NetC57_2 -> GND
- R47 pad 1: GND -> /CONN/LCD_BL_FB
- R47 pad 2: LCD_BL_FB -> GND
- R48 pad 1: GND -> /HOST_RD
- R48 pad 2: HOST_RD -> GND
- R49 pad 1: NetCN3_29 -> Net-(CN3-Pad28)
- R49 pad 2: LCD_BL_FB -> /CONN/LCD_BL_FB
- R50 pad 1: NetCN3_28 -> Net-(CN3-Pad29)
- R50 pad 2: LCD_BL_FB -> /CONN/LCD_BL_FB
- R53 pad 1: GND -> /FPGA/BL_DIM
- R53 pad 2: BL_DIM -> GND
- R54 pad 1: NetIC6_9 -> Net-(C80-Pad1)
- R54 pad 2: NetC80_1 -> Net-(IC6-Pad9)
- R55 pad 1: NetIC6_8 -> Net-(C81-Pad1)
- R55 pad 2: NetC81_1 -> Net-(IC6-Pad8)
- R67 pad 1: SDRAM_CLK_N -> /DDR/SDRAM_CLK_P
- R67 pad 2: SDRAM_CLK_P -> /DDR/SDRAM_CLK_N
- R68 pad 1: DDR_VREF -> +2V5
- R68 pad 2: P2V5 -> /DDR/DDR_VREF
- R69 pad 1: GND -> /DDR/DDR_VREF
- R69 pad 2: DDR_VREF -> GND
- R7 pad 1: TMS -> +3V3
- R7 pad 2: P3V3 -> /FPGA/TMS
- R72 pad 1: P2V5 -> +2V5
- R8 pad 1: CPU_RST -> /FPGA/CFG_CS
- R8 pad 2: CFG_CS -> /CPU_RST_N
- R9 pad 1: P2V5 -> Net-(IC1-Pad37)
- R9 pad 2: NetIC1_37 -> +2V5
- RA3 pad 1: GND -> /CONN/DSI_L0_P
- RA3 pad 2: DSI_CLK_P -> GND
- RA4 pad 1: DSI_CLK_N -> GND
- RA4 pad 2: GND -> /CONN/DSI_L0_N
- RA5 pad 1: DSI_CLK_N -> /CONN/DSI_L0_N
- RA5 pad 2: DSI_HS_CLK_N -> /FPGA/DSI_HS_N0
- RA51 pad 1: DSI_CLK_P -> /FPGA/DSI_LP_P0
- RA51 pad 2: DSI_LP_CLK_P -> /CONN/DSI_L0_P
- RA52 pad 1: DSI_CLK_P -> /CONN/DSI_L0_P
- RA52 pad 2: DSI_HS_CLK_P -> /FPGA/DSI_HS_P0
- RA6 pad 1: DSI_LP_CLK_N -> /CONN/DSI_L0_N
- RA6 pad 2: DSI_CLK_N -> /FPGA/DSI_LP_N0
- RB3 pad 1: GND -> /CONN/DSI_L1_P
- RB3 pad 2: DSI_L3_P -> GND
- RB4 pad 1: DSI_L3_N -> GND
- RB4 pad 2: GND -> /CONN/DSI_L1_N
- RB5 pad 1: DSI_L3_N -> /CONN/DSI_L1_N
- RB5 pad 2: DSI_HS_N3 -> /FPGA/DSI_HS_N1
- RB51 pad 1: DSI_L3_P -> /FPGA/DSI_LP_P1
- RB51 pad 2: DSI_LP_P3 -> /CONN/DSI_L1_P
- RB52 pad 1: DSI_L3_P -> /CONN/DSI_L1_P
- RB52 pad 2: DSI_HS_P3 -> /FPGA/DSI_HS_P1
- RB6 pad 1: DSI_LP_N3 -> /CONN/DSI_L1_N
- RB6 pad 2: DSI_L3_N -> /FPGA/DSI_LP_N1
- RC3 pad 1: GND -> /CONN/DSI_L2_P
- RC3 pad 2: DSI_L2_P -> GND
- RC4 pad 1: DSI_L2_N -> GND
- RC4 pad 2: GND -> /CONN/DSI_L2_N
- RC5 pad 1: DSI_L2_N -> /CONN/DSI_L2_N
- RC51 pad 1: DSI_L2_P -> /FPGA/DSI_LP_P2
- RC51 pad 2: DSI_LP_P2 -> /CONN/DSI_L2_P
- RC52 pad 1: DSI_L2_P -> /CONN/DSI_L2_P
- RC6 pad 1: DSI_LP_N2 -> /CONN/DSI_L2_N
- RC6 pad 2: DSI_L2_N -> /FPGA/DSI_LP_N2
- RD3 pad 1: GND -> /CONN/DSI_L3_P
- RD3 pad 2: DSI_L1_P -> GND
- RD4 pad 1: DSI_L1_N -> GND
- RD4 pad 2: GND -> /CONN/DSI_L3_N
- RD5 pad 1: DSI_L1_N -> /CONN/DSI_L3_N
- RD5 pad 2: DSI_HS_N1 -> /FPGA/DSI_HS_N3
- RD51 pad 1: DSI_L1_P -> /FPGA/DSI_LP_P3
- RD51 pad 2: DSI_LP_P1 -> /CONN/DSI_L3_P
- RD52 pad 1: DSI_L1_P -> /CONN/DSI_L3_P
- RD52 pad 2: DSI_HS_P1 -> /FPGA/DSI_HS_P3
- RD6 pad 1: DSI_LP_N1 -> /CONN/DSI_L3_N
- RD6 pad 2: DSI_L1_N -> /FPGA/DSI_LP_N3
- RE3 pad 1: GND -> /CONN/DSI_CLK_P
- RE3 pad 2: DSI_L0_P -> GND
- RE4 pad 1: DSI_L0_N -> GND
- RE4 pad 2: GND -> /CONN/DSI_CLK_N
- RE5 pad 1: DSI_L0_N -> /CONN/DSI_CLK_N
- RE5 pad 2: DSI_HS_N0 -> /FPGA/DSI_HS_CLK_N
- RE51 pad 1: DSI_L0_P -> /FPGA/DSI_LP_CLK_P
- RE51 pad 2: DSI_LP_P0 -> /CONN/DSI_CLK_P
- RE52 pad 1: DSI_L0_P -> /CONN/DSI_CLK_P
- RE52 pad 2: DSI_HS_P0 -> /FPGA/DSI_HS_CLK_P
- RE6 pad 1: DSI_LP_N0 -> /CONN/DSI_CLK_N
- RE6 pad 2: DSI_L0_N -> /FPGA/DSI_LP_CLK_N
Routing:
- net P3V3: track 115.8 -> 0.00 mm, vias 29 -> 0
- net +3V3: track 0.00 -> 115.6 mm, vias 0 -> 29
- net +2V5: track 0.00 -> 65.3 mm, vias 0 -> 20
- net P2V5: track 64.6 -> 0.00 mm, vias 20 -> 0
- net /SCL: track 0.00 -> 61.6 mm, vias 0 -> 2
- net SCL: track 61.5 -> 0.00 mm, vias 2 -> 0
- net SDA: track 56.9 -> 0.00 mm, vias 1 -> 0
- net /SDA: track 0.00 -> 56.8 mm, vias 0 -> 1
- net DDR_VREF: track 54.5 -> 0.00 mm, vias 4 -> 0
- net /DDR/DDR_VREF: track 0.00 -> 54.5 mm, vias 0 -> 4
- net CPU_RST: track 54.3 -> 0.00 mm, vias 6 -> 0
- net /CPU_RST_N: track 0.00 -> 54.3 mm, vias 0 -> 6
- net HDMI_P5V: track 50.7 -> 0.00 mm, vias 2 -> 0
- net /HDMI_IN/HDMI_P5V: track 0.00 -> 50.5 mm, vias 0 -> 2
- net LCD_BL_FB: track 48.6 -> 0.00 mm, vias 4 -> 0
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- added copper zone on PWR, net +1V2
- added copper zone on PWR, net +1V8
- added copper zone on B.Cu, net +2V5
- added copper zone on PWR, net +2V5
- added copper zone on PWR, net +3V3
- added copper zone on B.Cu, net +5V
- added copper zone on GND, net GNDA
- added copper zone on PWR, net VDDA
- removed copper zone on PWR, net P1V2
- removed copper zone on PWR, net P1V8
- removed copper zone on B.Cu, net P2V5
- removed copper zone on PWR, net P2V5
- removed copper zone on PWR, net P3V3
- removed copper zone on B.Cu, net P5V_IN
- removed copper zone on PWR, net VI_AVDD
- removed copper zone on GND, net VI_GND
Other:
- board text added: "Copyright 2013-2017 twl <twlostow@printf.cc> This documentation describes Open Hardware and is licensed under the CERN OHL v. 1.2. You may redistribute and modify this documentation under the terms of the CERN OHL v.1.2. (http://ohwr.org/CERNOHL). This documentation is distributed WITHOUT ANY EXPRESS OR IMPLIED WARRANTY, INCLUDING OF MERCHANTABILITY, SATISFACTORY QUALITY AND FITNESS FOR A PARTICU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"
- board text added: "HDMI DSI Shield"
- board text added: "JTAG"
- board text added: "PCB Main Board"
